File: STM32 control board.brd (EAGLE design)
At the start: 130 x 100 mm, 113 parts, among them J1 PJ-063BH, J10 S10B-PH, J11 S10B-PH, J12 S10B-PH, J13 S10B-PH, J14 S3B-PH, J15 S3B-PH, J16 S3B-PH, J17 S3B-PH, J18 DG301-4P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

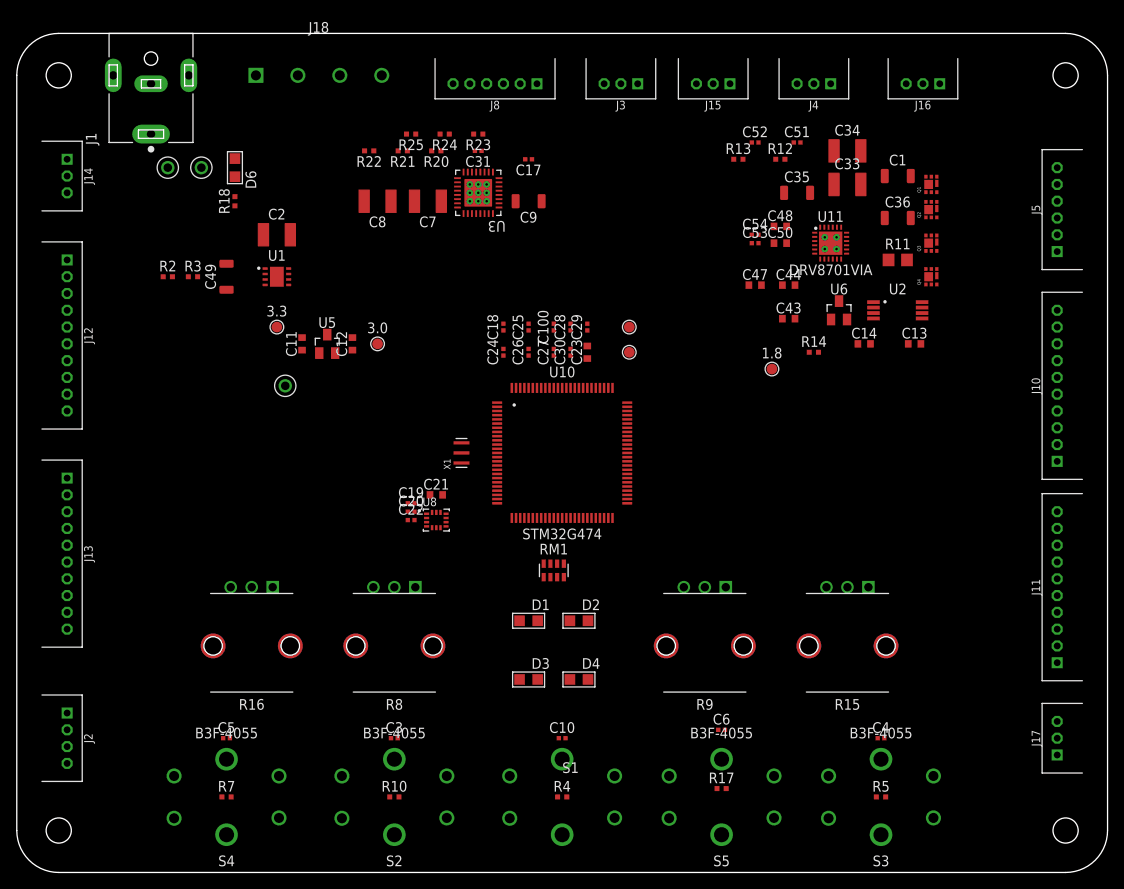
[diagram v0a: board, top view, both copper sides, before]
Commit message: Placed connectors as i see
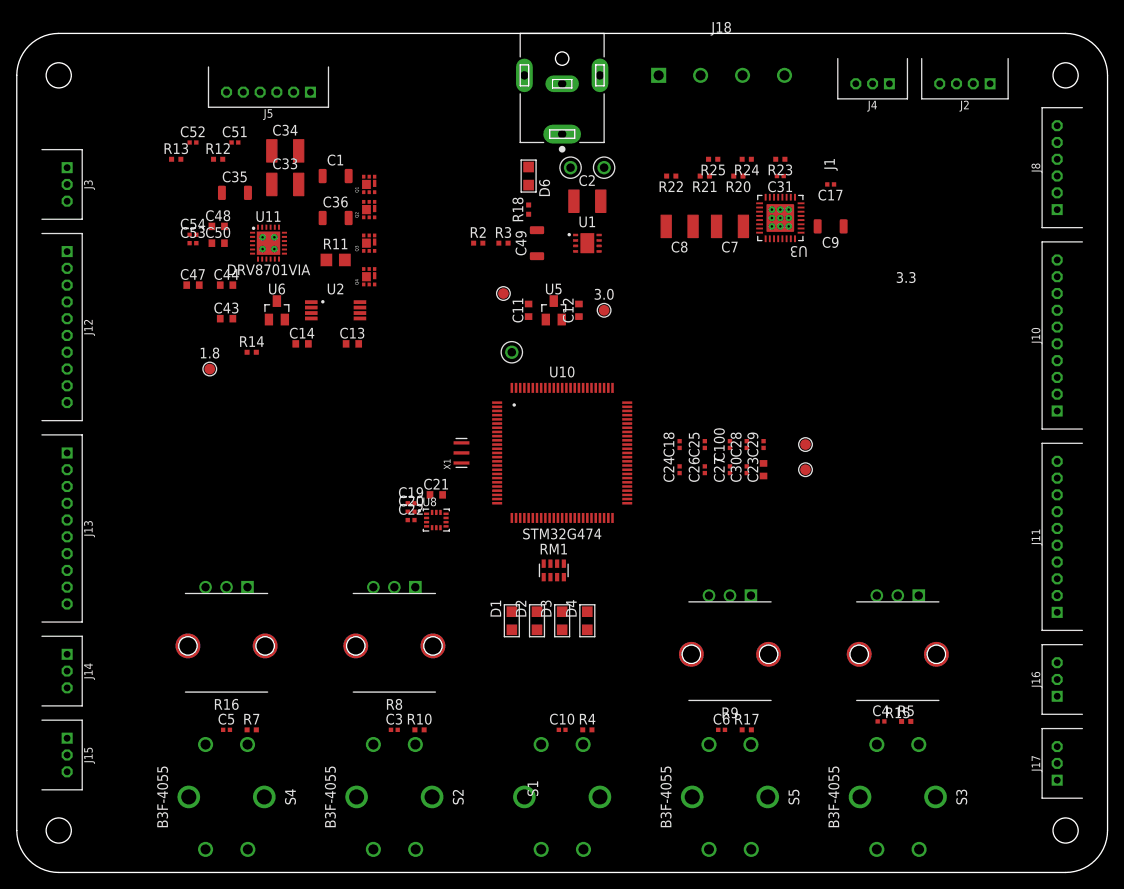
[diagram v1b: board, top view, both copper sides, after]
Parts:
- moved J2 132.4 mm to (113.0, 94.0), turned to 180 degrees
- moved J15 111.0 mm to (6.00, 14.0), turned to 270 degrees
- moved J5 95.0 mm to (30.0, 93.0), turned to 180 degrees
- moved J16 72.8 mm to (124.0, 23.0), turned to 90 degrees
- moved J8 67.7 mm to (124.0, 84.0), turned to 90 degrees
- moved J3 67.1 mm to (6.00, 82.0), turned to 270 degrees
- moved C1 67.0 mm to (38.0, 83.0)
- moved C13 67.0 mm to (40.0, 63.0)
- moved C14 67.0 mm to (34.0, 63.0)
- moved C33 67.0 mm to (32.0, 82.0)
- moved C34 67.0 mm to (32.0, 86.0)
- moved C35 67.0 mm to (26.0, 81.0)
- moved C36 67.0 mm to (38.0, 78.0)
- moved C43 67.0 mm to (25.0, 66.0)
- moved C44 67.0 mm to (25.0, 70.0)
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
